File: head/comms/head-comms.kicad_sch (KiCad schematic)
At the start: 26 parts, among them J1 conn_head_main, J3 USB_C_Receptacle_USB2.0_16P, J4 conn_chest, U1 LM66200, U2 SP48xE, U3 USBLC6-2SC6, U4 RP509x

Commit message: finishing touches
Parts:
- C1, C3, C48, C51, C60, R4, R5, R7, R9: LCSC (none) -> *
- C2: value 0.1u -> 100n; LCSC (none) -> *
- H1, H2, H3, H4, R1: LCSC (none) -> -
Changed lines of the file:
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@@
 		(rev "1")
 		(company "team noon")
-		(comment 1 "NanoID: rI02tsXA")
+		(comment 1 "NanoID: GRG4UQ")
 		(comment 3 "github.com/team-noon/hw1")
 		(comment 4 "Drawn By: Sam")
@@
 			)
 		)
+		(property "LCSC" "-"
+			(at 83.82 86.36 0)
+			(hide yes)
+			(show_name no)
+			(do_not_autoplace no)
+			(effects
+				(font
+					(size 1.27 1.27)
+				)
+			)
+		)
 		(pin "1"
 		)
@@
 			)
 		)
+		(property "LCSC" "-"
+			(at 130.81 87.63 0)
+			(hide yes)
+			(show_name no)
+			(do_not_autoplace no)
+			(effects
+				(font
+					(size 1.27 1.27)
+				)
+			)
+		)
 		(instances
 			(project "head-comms"
@@
 			)
 		)
+		(property "LCSC" "*"
+			(at 60.96 119.38 90)
+			(hide yes)
+			(show_name no)
+			(do_not_autoplace no)
+			(effects
+				(font
+					(size 1.27 1.27)
+				)
+			)
+		)
 		(pin "1"
 		)
@@
 			)
 		)
+		(property "LCSC" "-"
+			(at 146.05 87.63 0)
+			(hide yes)
+			(show_name no)
+			(do_not_autoplace no)
+			(effects
+				(font
+					(size 1.27 1.27)
+				)
+			)
+		)
 		(instances
 			(project "head-comms"
@@
 			)
 		)
+		(property "LCSC" "-"
+			(at 140.97 87.63 0)
+			(hide yes)
+			(show_name no)
+			(do_not_autoplace no)
+			(effects
+				(font
+					(size 1.27 1.27)
+				)
+			)
+		)
 		(instances
 			(project "head-comms"
@@
 			)
 		)
+		(property "LCSC" "*"
+			(at 76.2 115.57 0)
+			(hide yes)
+			(show_name no)
+			(do_not_autoplace no)
+			(effects
+				(font
+					(size 1.27 1.27)
+				)
+			)
+		)
 		(pin "1"
 		)
@@
 			)
 		)
+		(property "LCSC" "*"
+			(at 68.58 115.57 90)
+			(hide yes)
+			(show_name no)
+			(do_not_autoplace no)
+			(effects
+				(font
+					(size 1.27 1.27)
+				)
+			)
+		)
 		(pin "1"
 		)
@@
 			)
 		)
+		(property "LCSC" "*"
+			(at 53.34 62.23 0)
+			(hide yes)
+			(show_name no)
+			(do_not_autoplace no)
+			(effects
+				(font
+					(size 1.27 1.27)
+				)
+			)
+		)
 		(pin "2"
 		)
@@
 			)
 		)
-		(property "Value" "0.1u"
+		(property "Value" "100n"
 			(at 82.55 87.6299 0)
 			(hide yes)
@@
 			)
 		)
+		(property "LCSC" "*"
+			(at 78.74 86.36 0)
+			(hide yes)
+			(show_name no)
+			(do_not_autoplace no)
+			(effects
+				(font
+					(size 1.27 1.27)
+				)
+			)
+		)
 		(pin "2"
 		)
@@
 			)
 		)
+		(property "LCSC" "*"
+			(at 49.53 62.23 0)
+			(hide yes)
+			(show_name no)
+			(do_not_autoplace no)
+			(effects
+				(font
+					(size 1.27 1.27)
+				)
+			)
+		)
 		(pin "2"
 		)
@@
 			)
 		)
+		(property "LCSC" "*"
+			(at 73.66 86.36 0)
+			(hide yes)
+			(show_name no)
+			(do_not_autoplace no)
+			(effects
+				(font
+					(size 1.27 1.27)
+				)
+			)
+		)
 		(pin "2"
 		)
@@
 			)
 		)
+		(property "LCSC" "-"
+			(at 135.89 87.63 0)
+			(hide yes)
+			(show_name no)
+			(do_not_autoplace no)
+			(effects
+				(font
+					(size 1.27 1.27)
+				)
+			)
+		)
 		(instances
 			(project "head-comms"
@@
 			)
 		)
+		(property "LCSC" "*"
+			(at 68.58 119.38 90)
+			(hide yes)
+			(show_name no)
+			(do_not_autoplace no)
+			(effects
+				(font
+					(size 1.27 1.27)
+				)
+			)
+		)
 		(pin "2"
 		)
@@
 			)
 		)
+		(property "LCSC" "*"
+			(at 31.75 115.57 0)
+			(hide yes)
+			(show_name no)
+			(do_not_autoplace no)
+			(effects
+				(font
+					(size 1.27 1.27)
+				)
+			)
+		)
 		(pin "1"
 		)
@@
 			(at 26.67 115.57 0)
 			(hide yes)
+			(show_name no)
+			(do_not_autoplace no)
+			(effects
+				(font
+					(size 1.27 1.27)
+				)
+			)
+		)
+		(property "LCSC" "*"
+			(at 26.67 115.57 0)
+			(hide yes)

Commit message: fix missing ESD diode
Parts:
- removed D10: ESD, Diode_SMD:D_SOD-882, symbol Device:D
- added D10: ESD5Zxx, Diode_SMD:D_SOD-523, symbol Diode:ESD5Zxx
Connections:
- net GND: now also D10.2 (A)
- net VBUS: now also D10.1 (K)
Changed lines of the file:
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@@
 	(wire
 		(pts
-			(xy 29.21 97.79) (xy 24.13 97.79)
-		)
-		(stroke
-			(width 0)
-			(type default)
-		)
-	)
-	(wire
-		(pts
 			(xy 36.83 87.63) (xy 36.83 90.17)
 		)
@@
 	(wire
 		(pts
+			(xy 24.13 97.79) (xy 29.21 97.79)
+		)
+		(stroke
+			(width 0)
+			(type default)
+		)
+	)
+	(wire
+		(pts
 			(xy 36.83 90.17) (xy 45.72 90.17)
 		)
@@
 	)
 	(symbol
-		(lib_id "Device:D")
-		(at 40.64 87.63 180)
-		(unit 1)
-		(body_style 1)
-		(exclude_from_sim no)
-		(in_bom yes)
-		(on_board yes)
-		(in_pos_files yes)
-		(dnp no)
-		(property "Reference" "D10"
-			(at 40.64 92.71 0)
-			(show_name no)
-			(do_not_autoplace no)
-			(effects
-				(font
-					(size 1.27 1.27)
-				)
-			)
-		)
-		(property "Value" "ESD"
-			(at 39.3701 90.17 90)
-			(hide yes)
-			(show_name no)
-			(do_not_autoplace no)
-			(effects
-				(font
-					(size 1.27 1.27)
-				)
-				(justify left)
-			)
-		)
-		(property "Footprint" "Diode_SMD:D_SOD-882"
-			(at 40.64 87.63 0)
-			(hide yes)
-			(show_name no)
-			(do_not_autoplace no)
-			(effects
-				(font
-					(size 1.27 1.27)
-				)
-			)
-		)
-		(property "Datasheet" ""
-			(at 40.64 87.63 0)
-			(hide yes)
-			(show_name no)
-			(do_not_autoplace no)
-			(effects
-				(font
-					(size 1.27 1.27)
-				)
-			)
-		)
-		(property "Description" "Diode"
-			(at 40.64 87.63 0)
-			(hide yes)
-			(show_name no)
-			(do_not_autoplace no)
-			(effects
-				(font
-					(size 1.27 1.27)
-				)
-			)
-		)
-		(property "Sim.Device" "D"
-			(at 40.64 87.63 0)
-			(hide yes)
-			(show_name no)
-			(do_not_autoplace no)
-			(effects
-				(font
-					(size 1.27 1.27)
-				)
-			)
-		)
-		(property "Sim.Pins" "1=K 2=A"
-			(at 40.64 87.63 0)
-			(hide yes)
-			(show_name no)
-			(do_not_autoplace no)
-			(effects
-				(font
-					(size 1.27 1.27)
-				)
-			)
-		)
-		(pin "1"
-		)
-		(pin "2"
-		)
-		(instances
-			(project "head-comms"
-				(path "/a00faf05-8464-4a38-a338-9c67c7b17254"
-					(reference "D10")
-					(unit 1)
-				)
-			)
-		)
-	)
-	(symbol
 		(lib_id "power:+5V")
 		(at 92.71 25.4 270)
@@
 					(unit 1)
 				)
+			)
+		)
+	)
+	(symbol
+		(lib_id "Diode:ESD5Zxx")
+		(at 40.64 87.63 180)
+		(unit 1)
+		(body_style 1)
+		(exclude_from_sim no)
+		(in_bom yes)
+		(on_board yes)
+		(in_pos_files yes)
+		(dnp no)
+		(property "Reference" "D10"
+			(at 40.64 92.71 0)
+			(show_name no)
+			(do_not_autoplace no)
+			(effects
+				(font
+					(size 1.27 1.27)
+				)
+			)
+		)
+		(property "Value" "ESD5Zxx"
+			(at 40.64 91.44 0)
+			(hide yes)
+			(show_name no)
+			(do_not_autoplace no)
+			(effects
+				(font
+					(size 1.27 1.27)
+				)
+			)
+		)
+		(property "Footprint" "Diode_SMD:D_SOD-523"
+			(at 40.64 83.185 0)
+			(hide yes)
+			(show_name no)
+			(do_not_autoplace no)
+			(effects
+				(font
+					(size 1.27 1.27)
+				)
+			)
+		)
+		(property "Datasheet" "https://www.onsemi.com/pdf/datasheet/esd5z2.5t1-d.pdf"
+			(at 40.64 87.63 0)
+			(hide yes)
+			(show_name no)
+			(do_not_autoplace no)
+			(effects
+				(font
+					(size 1.27 1.27)
+				)
+			)
+		)
+		(property "Description" "ESD Protection Diode, SOD-523"
+			(at 40.64 87.63 0)
+			(hide yes)
+			(show_name no)
+			(do_not_autoplace no)
+			(effects
+				(font
+					(size 1.27 1.27)
+				)
+			)
+		)
+		(property "LCSC" "C82323"
+			(at 40.64 87.63 0)
+			(hide yes)
+			(show_name no)
+			(do_not_autoplace no)
+			(effects
+				(font
+					(size 1.27 1.27)
+				)
+			)
+		)
+		(pin "2"
+		)
+		(pin "1"
+		)
+		(instances
+			(project "head-comms"
+				(path "/a00faf05-8464-4a38-a338-9c67c7b17254"
+					(reference "D10")
+					(unit 1)
+				)

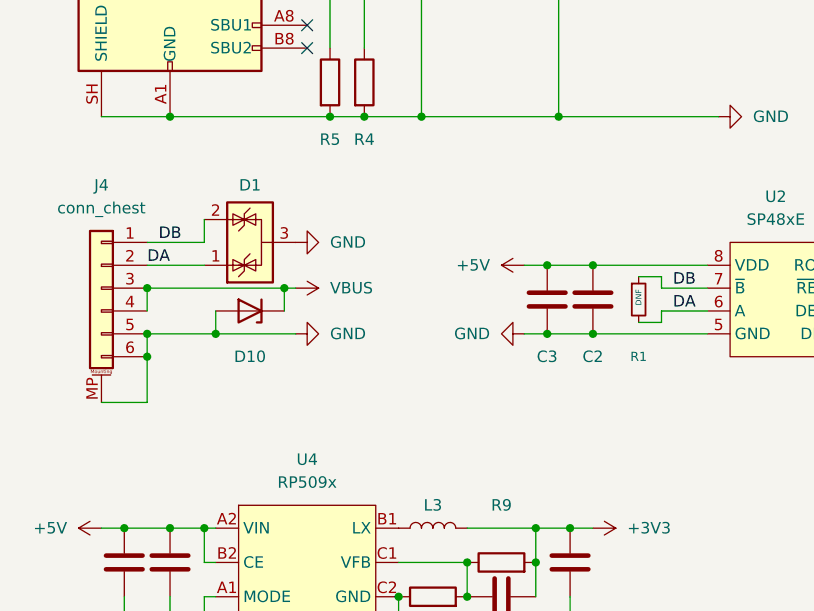
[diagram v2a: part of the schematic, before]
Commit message: larger traces, swapped connector
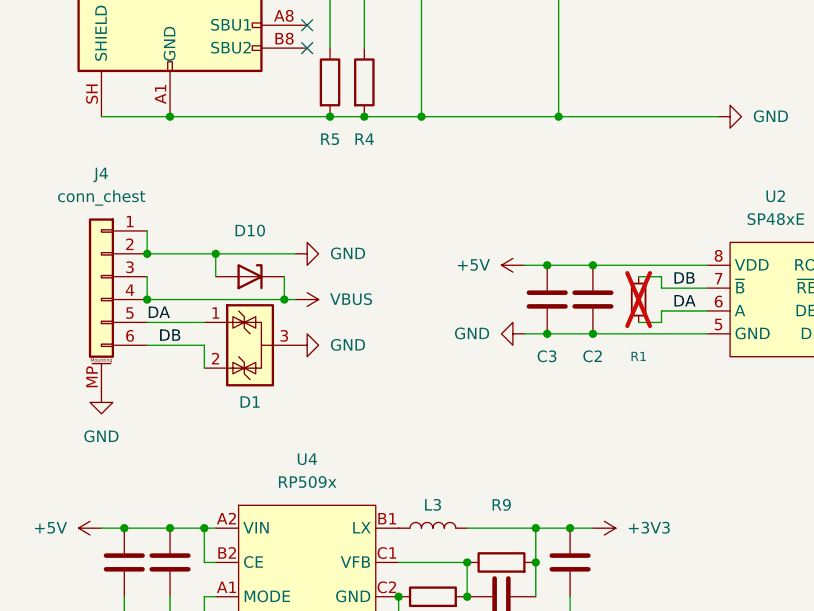
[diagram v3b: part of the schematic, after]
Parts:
- J4: footprint misc:A1257WV-S-6P-LCP -> Connector_JST:JST_SH_SM06B-SRSS-TB_1x06-1MP_P1.00mm_Horizontal; LCSC C225129 -> C160405
- R1: value 120 (DNF) -> 120; now not fitted; now in the parts list
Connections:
- net DA: now also J4.5 (Pin_5); no longer J4.2 (Pin_2)
- net DB: now also J4.6 (Pin_6); no longer J4.1 (Pin_1)
- net GND: now also J4.1 (Pin_1), J4.2 (Pin_2); no longer J4.5 (Pin_5), J4.6 (Pin_6)
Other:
- note removed: "DNF"
- moved on the sheet: D1, D10
